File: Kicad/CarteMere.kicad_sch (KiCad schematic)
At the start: 55 parts, among them J1 Conn_01x06, J10 Conn_01x04, J12 Conn_01x06, J13 Conn_01x06, J14 Conn_01x04, J15 Conn_01x04, J16 Conn_01x04, J18 Conn_01x06, J19 Conn_01x06, J2 Conn_01x10, J21 Conn_01x04, J22 Conn_01x04, J23 Conn_01x04, J24 Conn_01x02, J25 Conn_01x06, J26 Conn_01x02, J27 Conn_01x06, J28 Conn_01x06, J29 Conn_01x06, J3 Conn_01x10, J30 Conn_01x06, J31 Conn_01x02, J32 Conn_01x09, J33 Conn_01x05, J34 Conn_01x05, J35 Conn_01x05, J36 Conn_01x05, J37 Conn_01x05, J39 Conn_01x09, J4 Conn_01x10, J40 Conn_01x09, J41 Conn_01x05, J42 Conn_01x05, J43 Conn_01x05, J44 Conn_01x05, J45 Conn_01x05, J46 Conn_01x05, J47 Conn_01x05, J49 Conn_01x02, J5 Conn_01x06, J6 Conn_01x06, J7 Conn_01x06, J8 Conn_01x04, J9 Conn_01x04

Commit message: ajout spi et maj readme
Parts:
- removed J10, J15, J16, J21, J23, J8: Conn_01x04, Connector_PinHeader_2.54mm:PinHeader_1x04_P2.54mm_Vertical, symbol Connector_Generic:Conn_01x04
- removed J2, J3, J4: Conn_01x10, Connector_PinHeader_2.54mm:PinHeader_1x10_P2.54mm_Vertical, symbol Connector_Generic:Conn_01x10
- removed J24, J26, J31: Conn_01x02, Connector_PinHeader_2.54mm:PinHeader_1x02_P2.54mm_Vertical, symbol Connector_Generic:Conn_01x02
- added J10: Conn_01x05, Connector_JST:JST_EH_B5B-EH-A_1x05_P2.50mm_Vertical, symbol Connector_Generic:Conn_01x05
- added J11, J16, J17: Conn_01x07, Connector_JST:JST_EH_B7B-EH-A_1x07_P2.50mm_Vertical, symbol Connector_Generic:Conn_01x07
- added J2, J3, J8: Conn_01x07, Connector_PinHeader_2.54mm:PinHeader_1x07_P2.54mm_Vertical, symbol Connector_Generic:Conn_01x07
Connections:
- net +3.3V: now also J10.1 (Pin_1), J11.7 (Pin_7), J16.7 (Pin_7), J17.7 (Pin_7), J2.1 (Pin_1), J2.2 (Pin_2), J2.3 (Pin_3), J2.4 (Pin_4), J2.5 (Pin_5), J2.6 (Pin_6), J2.7 (Pin_7)
- net GND: now also J10.2 (Pin_2), J10.4 (Pin_4), J11.6 (Pin_6), J16.6 (Pin_6), J17.6 (Pin_6), J3.1 (Pin_1), J3.2 (Pin_2), J3.3 (Pin_3), J3.4 (Pin_4), J3.5 (Pin_5), J3.6 (Pin_6), J3.7 (Pin_7)
- net GPIO_PD11: now also J8.7 (Pin_7)
- net GPIO_PD12: now also J8.6 (Pin_6)
- net GPIO_PD13: now also J8.5 (Pin_5)
- net GPIO_PG4: now also J8.4 (Pin_4)
- net GPIO_PG5: now also J8.3 (Pin_3)
- net GPIO_PG6: now also J8.2 (Pin_2)
- net GPIO_PG7: now also J8.1 (Pin_1)
- net GPIO_PG0 renamed GPIO_PF14
- net GPIO_PG1 renamed GPIO_PF15
- new net GPIO_PB10: J16.2 (Pin_2)
- new net GPIO_PB11: J16.1 (Pin_1)
- new net GPIO_PC13: J11.1 (Pin_1)
- new net GPIO_PH2: J17.2 (Pin_2)
- new net GPIO_PH3: J17.1 (Pin_1)
- new net GPIO_PI8: J11.2 (Pin_2)
- new net SPI4_MISO: J11.5 (Pin_5)
- new net SPI4_MOSI: J11.4 (Pin_4)
- new net SPI4_SCK: J11.3 (Pin_3)
- new net SPI5_MISO: J16.5 (Pin_5)
- new net SPI5_MOSI: J16.4 (Pin_4)
- new net SPI5_SCK: J16.3 (Pin_3)
- new net SPI6_MISO: J17.5 (Pin_5)
- new net SPI6_MOSI: J17.4 (Pin_4)
- new net SPI6_SCK: J17.3 (Pin_3)
- new net UART9_RX: J10.5 (Pin_5)
- new net UART9_TX: J10.3 (Pin_3)
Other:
- sheet MCU ports: added GPIO_PB10, GPIO_PB11, GPIO_PC13, GPIO_PF14, GPIO_PF15, GPIO_PH2, GPIO_PH3, GPIO_PI8, SPI4_MISO, SPI4_MOSI, SPI4_SCK, SPI5_MISO, SPI5_MOSI, SPI5_SCK, SPI6_MISO, SPI6_MOSI, SPI6_SCK, UART9_RX, UART9_TX; removed ADC2_INP2, ADC2_INP6, GPIO_PG0, GPIO_PG1, GPIO_PI10, GPIO_PI11, GPIO_PI9, TIM3_CH1, TIM3_CH2, TIM3_CH3, TIM3_CH4, TIM8_CH1, TIM8_CH2, TIM8_CH3, TIM8_CH4
- note added: "SPI with PWR pins"
- note removed: "ADC2 with PWR pins"
- moved on the sheet: J14, J22, J33, J34, J35, J36, J37, J9

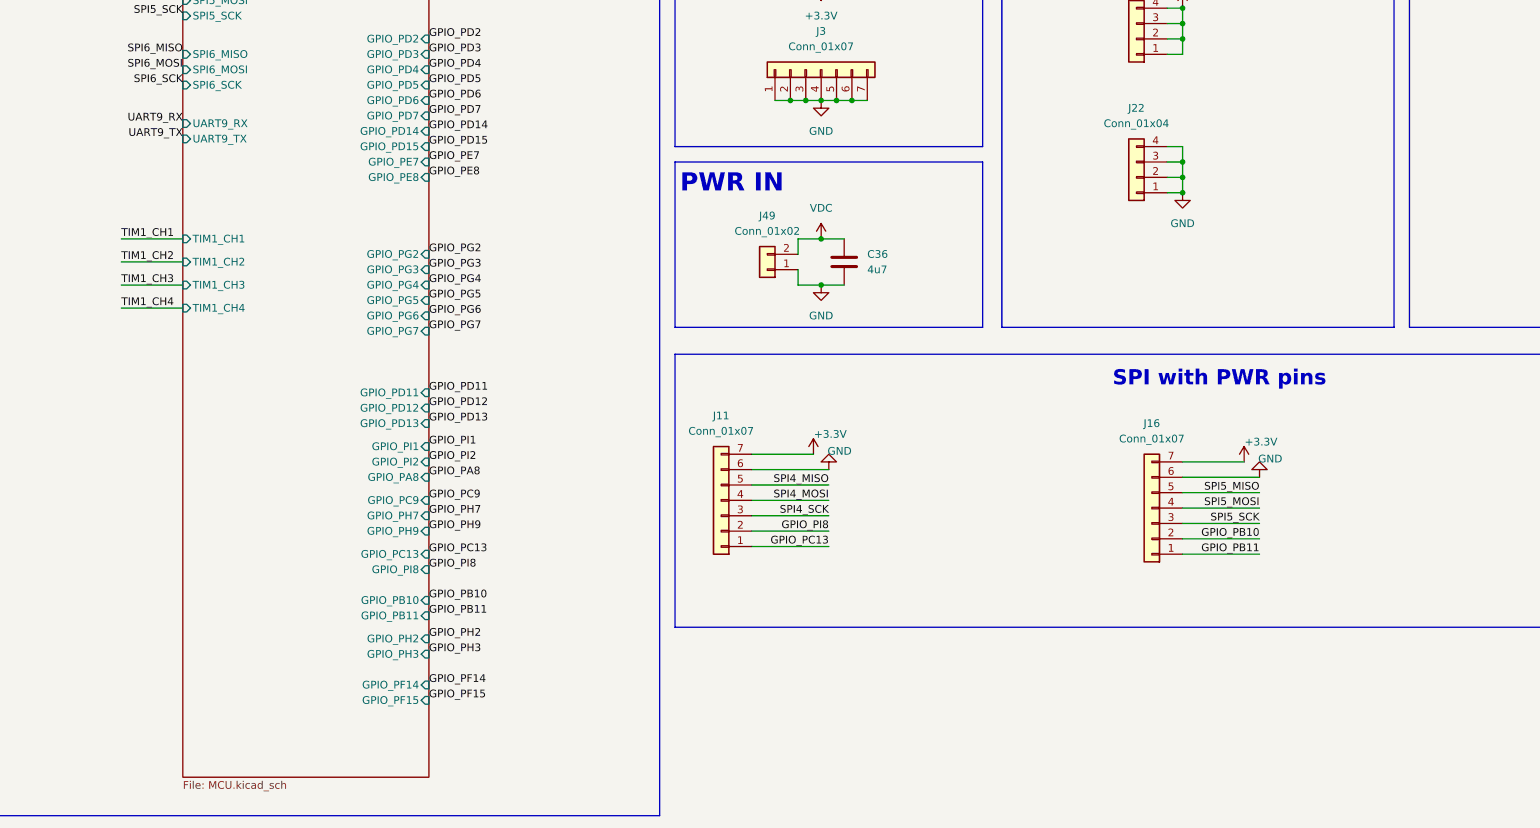
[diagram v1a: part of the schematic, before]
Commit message: ajout d'un connecteur SPI
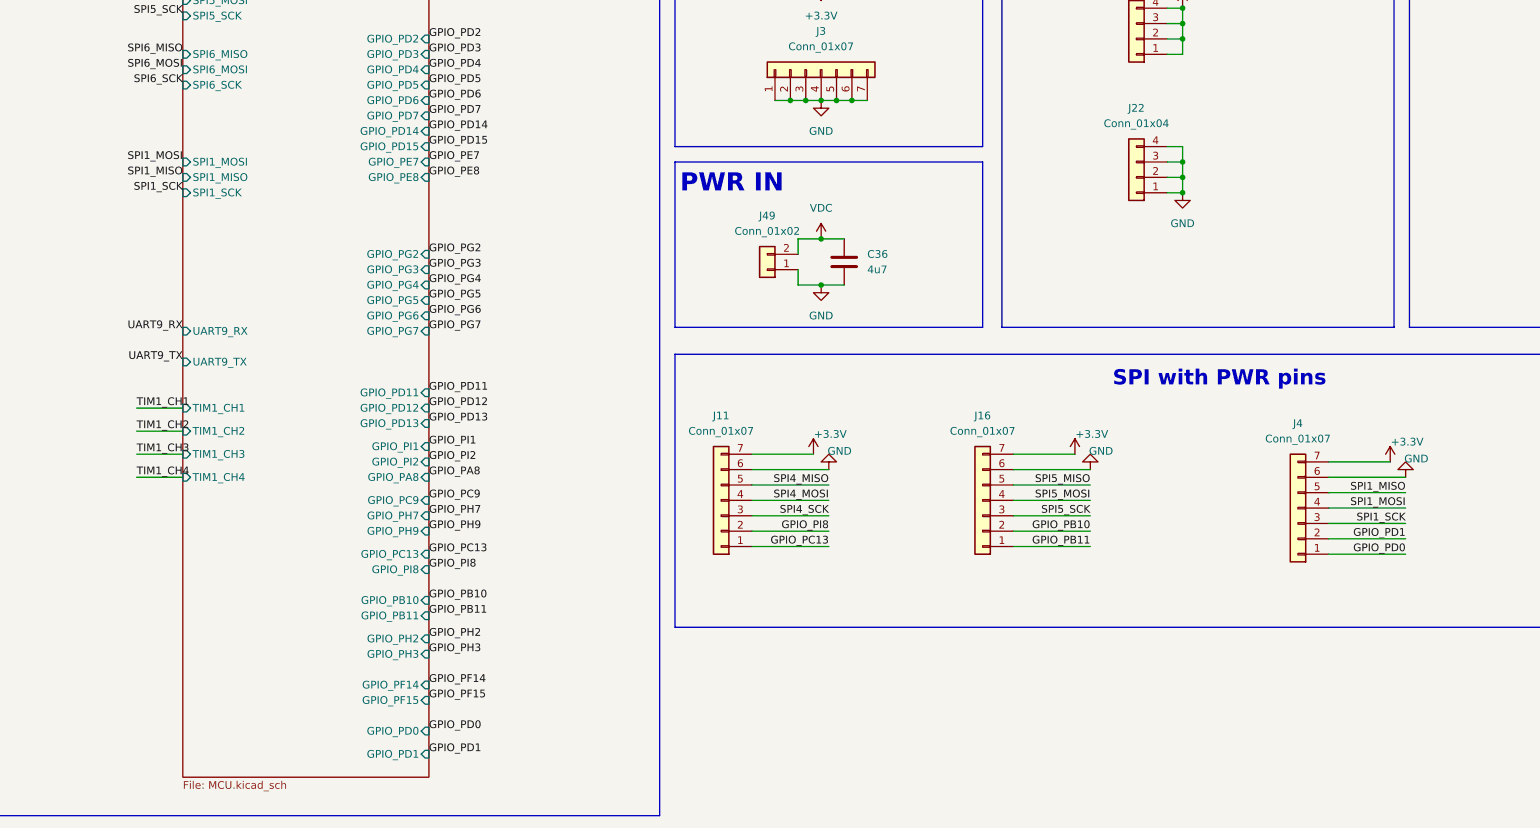
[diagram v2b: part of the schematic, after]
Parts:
- added J4: Conn_01x07, Connector_JST:JST_EH_B7B-EH-A_1x07_P2.50mm_Vertical, symbol Connector_Generic:Conn_01x07
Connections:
- net +3.3V: now also J4.7 (Pin_7)
- net GND: now also J4.6 (Pin_6)
- new net GPIO_PD0: J4.1 (Pin_1)
- new net GPIO_PD1: J4.2 (Pin_2)
- new net SPI1_MISO: J4.5 (Pin_5)
- new net SPI1_MOSI: J4.4 (Pin_4)
- new net SPI1_SCK: J4.3 (Pin_3)
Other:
- sheet MCU ports: added GPIO_PD0, GPIO_PD1, SPI1_MISO, SPI1_MOSI, SPI1_SCK; removed none
- moved on the sheet: J16
